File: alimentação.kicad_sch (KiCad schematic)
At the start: 10 parts, among them U2 LM317G, U3 AMS1117-5.0

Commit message: organização e legendas do esquemático
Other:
- moved on the sheet: C2, C3, C4, D1, R5, R6, R7, R8, U2, U3

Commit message: ajustes no layout e serigrafia
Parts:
- added C12: 10uFx50V, Capacitor_THT:CP_Radial_D5.0mm_P2.50mm, symbol Device:C_Polarized
- added U8: AMS1117-5.0, jlclib:SOT-223_L6.5-W3.5-P2.30-LS7.0-BR, symbol a_jlclib:AMS1117-5.0
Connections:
- net 7,5V_OUT: now also U8.3 (VIN)
- net GND: now also C12.2, U8.1 (GND)
- new net 5V_SERVO: C12.1, U8.2 (VOUT), U8.4 (VOUT)

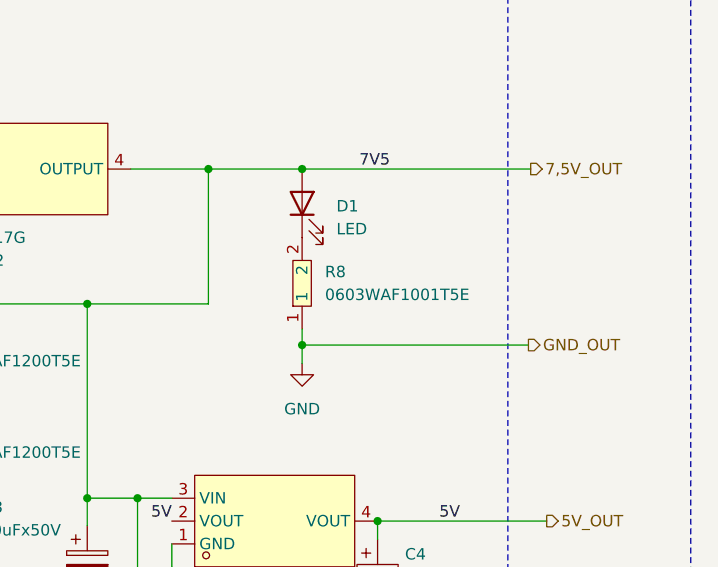
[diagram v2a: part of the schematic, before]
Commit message: ajusta circuitos de entrada, alimentação e saída e adiciona visualizações da PCB
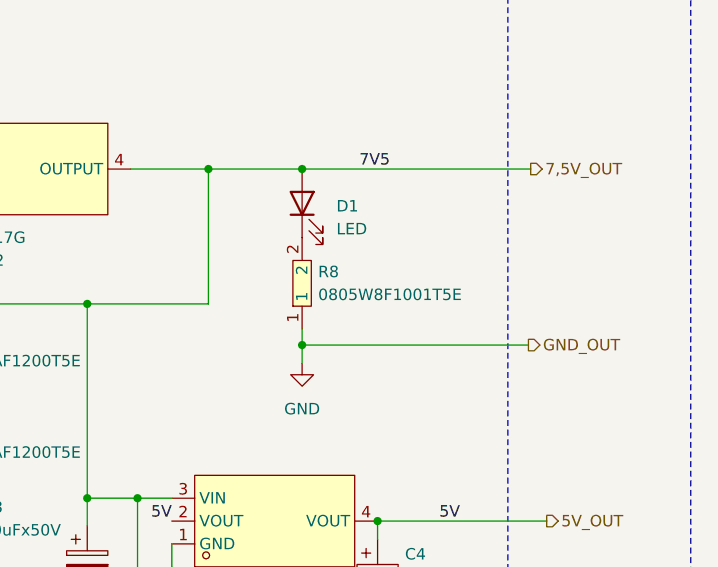
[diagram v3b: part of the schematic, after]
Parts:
- removed R8: 0603WAF1001T5E, jlclib:R0603, symbol a_jlclib:0603WAF1001T5E
- added R8: 0805W8F1001T5E, jlclib:R0805, symbol a_jlclib:0805W8F1001T5E
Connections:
- net GND: now also R8.1
- net at D1.1 (K): now also R8.2
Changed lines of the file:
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@@
+	)
+	(symbol
+		(lib_id "a_jlclib:0805W8F1001T5E")
+		(at 165.354 96.012 90)
+		(unit 1)
+		(exclude_from_sim no)
+		(in_bom yes)
+		(on_board yes)
+		(dnp no)
+		(fields_autoplaced yes)
+		(property "Reference" "R8"
+			(at 167.132 94.7419 90)
+			(effects
+				(font
+					(size 1.27 1.27)
+				)
+				(justify right)
+			)
+		)
+		(property "Value" "0805W8F1001T5E"
+			(at 167.132 97.2819 90)
+			(effects
+				(font
+					(size 1.27 1.27)
+				)
+				(justify right)
+			)
+		)
+		(property "Footprint" "jlclib:R0805"
+			(at 172.974 96.012 0)
+			(effects
+				(font
+					(size 1.27 1.27)
+				)
+				(hide yes)
+			)
+		)
+		(property "Datasheet" "https://lcsc.com/product-detail/Chip-Resistor-Surface-Mount-UniOhm_1KR-1001-1_C17513.html"
+			(at 175.514 96.012 0)
+			(effects
+				(font
+					(size 1.27 1.27)
+				)
+				(hide yes)
+			)
+		)
+		(property "Description" "1KΩ (1001) ±1%"
+			(at 165.354 96.012 0)
+			(effects
+				(font
+					(size 1.27 1.27)
+				)
+				(hide yes)
+			)
+		)
+		(property "Manufacturer" "UNI-ROYAL(厚声)"
+			(at 178.054 96.012 0)
+			(effects
+				(font
+					(size 1.27 1.27)
+				)
+				(hide yes)
+			)
+		)
+		(property "MPN" "0805W8F1001T5E"
+			(at 180.594 96.012 0)
+			(effects
+				(font
+					(size 1.27 1.27)
+				)
+				(hide yes)
+			)
+		)
+		(property "LCSC Part" "C17513"
+			(at 183.134 96.012 0)
+			(effects
+				(font
+					(size 1.27 1.27)
+				)
+				(hide yes)
+			)
+		)
+		(pin "2"
+		)
+		(pin "1"
+		)
+		(instances
+			(project "pcb-moduloDidaticoSCADA"
+				(path "/d871af36-cd7a-4e62-8016-cc5e63560ec7/c8e2f891-c1a6-4289-9136-24a9cda3131a"
+					(reference "R8")
+					(unit 1)
+				)
+			)
+		)
 	)
 	(symbol
@@
 					(unit 1)
 				)
-			)
-		)
-	)
-	(symbol
-		(lib_id "a_jlclib:0603WAF1001T5E")
-		(at 165.354 96.012 90)
-		(unit 1)
-		(exclude_from_sim no)
-		(in_bom yes)
-		(on_board yes)
-		(dnp no)
-		(fields_autoplaced yes)
-		(property "Reference" "R8"
-			(at 167.894 94.7419 90)
-			(effects
-				(font
-					(size 1.27 1.27)
-				)
-				(justify right)
-			)
-		)
-		(property "Value" "0603WAF1001T5E"
-			(at 167.894 97.2819 90)
-			(effects
-				(font
-					(size 1.27 1.27)
-				)
-				(justify right)
-			)
-		)
-		(property "Footprint" "jlclib:R0603"
-			(at 172.974 96.012 0)
-			(effects
-				(font
-					(size 1.27 1.27)
-				)
-				(hide yes)
-			)
-		)
-		(property "Datasheet" "https://lcsc.com/product-detail/Chip-Resistor-Surface-Mount-UniOhm_1KR-1001-1_C21190.html"
-			(at 175.514 96.012 0)
-			(effects
-				(font
-					(size 1.27 1.27)
-				)
-				(hide yes)
-			)
-		)
-		(property "Description" "1KΩ (1001) ±1%"
-			(at 165.354 96.012 0)
-			(effects
-				(font
-					(size 1.27 1.27)
-				)
-				(hide yes)
-			)
-		)
-		(property "Manufacturer" "UNI-ROYAL(厚声)"
-			(at 178.054 96.012 0)
-			(effects
-				(font
-					(size 1.27 1.27)
-				)
-				(hide yes)
-			)
-		)
-		(property "MPN" "0603WAF1001T5E"
-			(at 180.594 96.012 0)
-			(effects
-				(font
-					(size 1.27 1.27)
-				)
-				(hide yes)
-			)
-		)
-		(property "LCSC Part" "C21190"
-			(at 183.134 96.012 0)
-			(effects
-				(font
-					(size 1.27 1.27)
-				)
-				(hide yes)
-			)
-		)
-		(pin "2"
-		)
-		(pin "1"
-		)
-		(instances
-			(project ""
-				(path "/d871af36-cd7a-4e62-8016-cc5e63560ec7/c8e2f891-c1a6-4289-9136-24a9cda3131a"
-					(reference "R8")
-					(unit 1)
-				)
